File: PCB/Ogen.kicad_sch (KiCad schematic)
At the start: 17 parts, among them J1 Input, U1 PMW3360DM-T2QU, U2 TLV70019, U3 TXS0102DCU, U4 TXS0102DCU, U5 TXS0102DCU

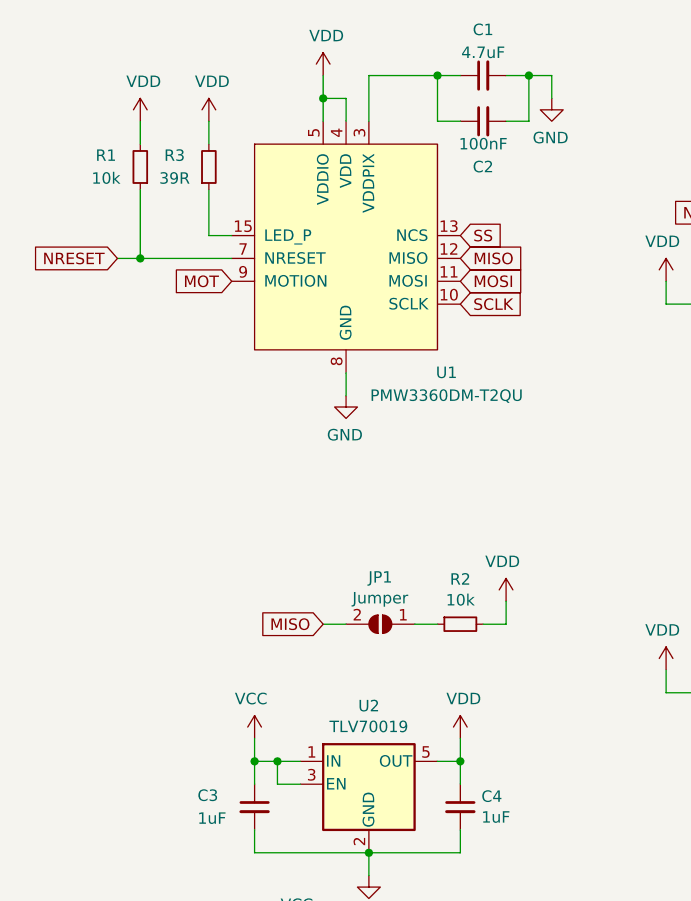
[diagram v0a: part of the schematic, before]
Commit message: ✨ ♻️ - Add metadata required to generate BOM and POS files for JLCPCB SMT assembly service (can use Fabrication Toolkit plugin to generate up to date BOM and POS). Add description to PCB and schema files. Replace TLV70019 (rupture) part by VRH1902LTX (in stock).
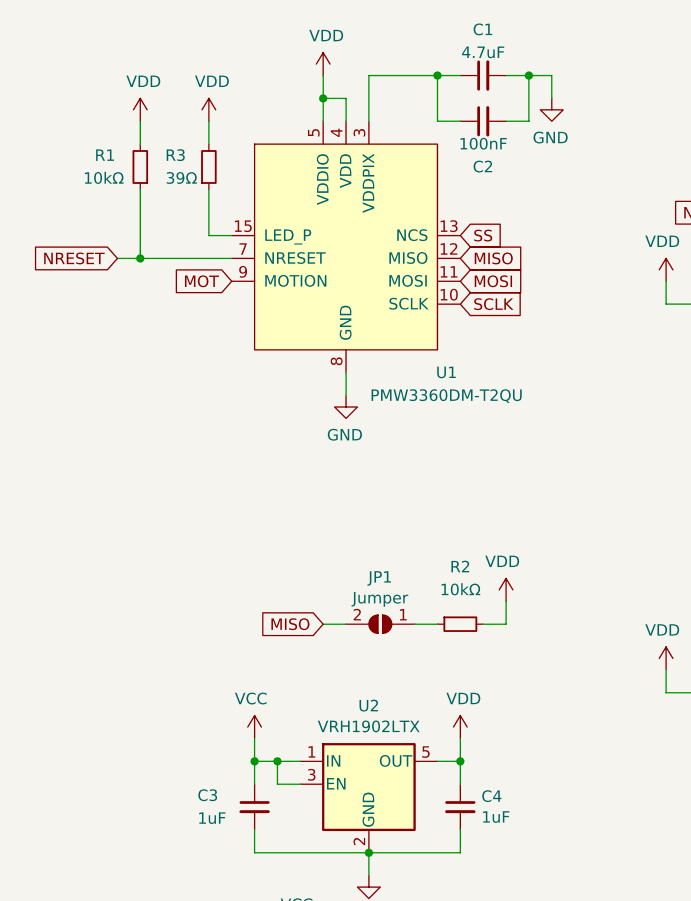
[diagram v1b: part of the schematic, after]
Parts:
- A1, H1, H2, J1, JP1: now left out of the parts list
- C1: LCSC Part # (none) -> C19666
- C2: LCSC Part # (none) -> C14663
- C3, C4: LCSC Part # (none) -> C15849
- R1, R2: value 10k -> 10kΩ; LCSC Part # (none) -> C25804
- R3: value 39R -> 39Ω; LCSC Part # (none) -> C227492
- U2: value TLV70019 -> VRH1902LTX; JLCPCB Rotation Offset (none) -> -90; LCSC Part # (none) -> C697975
- U3, U5: JLCPCB Rotation Offset (none) -> 180; LCSC Part # (none) -> C53434
- U4: JLCPCB Rotation Offset (none) -> 180; LCSC Part # (none) -> C9382C53434
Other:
- company: (none) -> Ariamelon
- title: (none) -> Ogen
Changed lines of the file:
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@@
 (kicad_sch (version 20211123) (generator eeschema)
   (paper "A4")
+  (title_block
+    (title "Ogen")
+    (date "2022-11-11")
+    (rev "V1.2")
+    (company "Ariamelon")
+  )
   (junction (at 50.8 106.68) (diameter 0) (color 0 0 0 0)
   )
@@
     (in_bom yes) (on_board yes) (fields_autoplaced)
     (property "Reference" "U2" (id 0) (at 50.8 90.3732 0))
-    (property "Value" "TLV70019" (id 1) (at 50.8 92.6846 0))
+    (property "Value" "VRH1902LTX" (id 1) (at 50.8 92.6846 0))
     (property "Footprint" "Package_TO_SOT_SMD:SOT-23-5" (id 2) (at 50.8 90.805 0)
       (effects (font (size 1.27 1.27) italic) hide)
     )
     (property "Datasheet" "http://www.ti.com/lit/ds/symlink/tlv700.pdf" (id 3) (at 50.8 97.79 0)
+      (effects (font (size 1.27 1.27)) hide)
+    )
+    (property "LCSC Part #" "C697975" (id 4) (at 50.8 99.06 0)
+      (effects (font (size 1.27 1.27)) hide)
+    )
+    (property "JLCPCB Rotation Offset" "-90" (id 5) (at 50.8 99.06 0)
       (effects (font (size 1.27 1.27)) hide)
     )
@@
   )
   (symbol (lib_id "Device:R_Small") (at 25.4 30.48 180) (unit 1)
-    (in_bom yes) (on_board yes) (fields_autoplaced)
-    (property "Reference" "R1" (id 0) (at 21.59 29.2099 0))
-    (property "Value" "10k" (id 1) (at 21.59 31.7499 0))
+    (in_bom yes) (on_board yes)
+    (property "Reference" "R1" (id 0) (at 20.32 29.21 0)
+      (effects (font (size 1.27 1.27)) (justify right))
+    )
+    (property "Value" "10kΩ" (id 1) (at 19.05 31.75 0)
+      (effects (font (size 1.27 1.27)) (justify right))
+    )
     (property "Footprint" "Resistor_SMD:R_0603_1608Metric" (id 2) (at 25.4 30.48 0)
       (effects (font (size 1.27 1.27)) hide)
     )
     (property "Datasheet" "~" (id 3) (at 25.4 30.48 0)
+      (effects (font (size 1.27 1.27)) hide)
+    )
+    (property "LCSC Part #" "C25804" (id 4) (at 25.4 30.48 0)
       (effects (font (size 1.27 1.27)) hide)
     )
@@
       (effects (font (size 1.27 1.27)) hide)
     )
+    (property "LCSC Part #" "C15849" (id 4) (at 60.96 101.6 0)
+      (effects (font (size 1.27 1.27)) hide)
+    )
     (pin "1")
     (pin "2")
@@
     )
     (property "Datasheet" "~" (id 3) (at 38.1 101.6 0)
+      (effects (font (size 1.27 1.27)) hide)
+    )
+    (property "LCSC Part #" "C15849" (id 4) (at 38.1 101.6 0)
       (effects (font (size 1.27 1.27)) hide)
     )
@@
       (effects (font (size 1.27 1.27)) hide)
     )
+    (property "LCSC Part #" "C19666" (id 4) (at 63.5 20.32 90)
+      (effects (font (size 1.27 1.27)) hide)
+    )
     (pin "1")
     (pin "2")
@@
       (effects (font (size 1.27 1.27)) hide)
     )
+    (property "LCSC Part #" "C14663" (id 4) (at 63.5 25.4 90)
+      (effects (font (size 1.27 1.27)) hide)
+    )
     (pin "1")
     (pin "2")
   )
   (symbol (lib_id "Device:R_Small") (at 33.02 30.48 0) (mirror x) (unit 1)
-    (in_bom yes) (on_board yes) (fields_autoplaced)
-    (property "Reference" "R3" (id 0) (at 29.21 29.2099 0))
-    (property "Value" "39R" (id 1) (at 29.21 31.7499 0))
+    (in_bom yes) (on_board yes)
+    (property "Reference" "R3" (id 0) (at 30.48 29.21 0)
+      (effects (font (size 1.27 1.27)) (justify right))
+    )
+    (property "Value" "39Ω" (id 1) (at 31.75 31.75 0)
+      (effects (font (size 1.27 1.27)) (justify right))
+    )
     (property "Footprint" "Resistor_SMD:R_0603_1608Metric" (id 2) (at 33.02 30.48 0)
       (effects (font (size 1.27 1.27)) hide)
@@
       (effects (font (size 1.27 1.27)) hide)
     )
+    (property "LCSC Part #" "C227492" (id 4) (at 33.02 30.48 0)
+      (effects (font (size 1.27 1.27)) hide)
+    )
     (pin "1")
     (pin "2")
   )
   (symbol (lib_id "Connector_Generic:Conn_01x08") (at 35.56 127 0) (mirror y) (unit 1)
-    (in_bom yes) (on_board yes) (fields_autoplaced)
+    (in_bom no) (on_board yes) (fields_autoplaced)
     (property "Reference" "J1" (id 0) (at 33.528 127.2032 0)
       (effects (font (size 1.27 1.27)) (justify left))
@@
   )
   (symbol (lib_id "Jumper:SolderJumper_2_Open") (at 52.07 81.28 0) (mirror y) (unit 1)
-    (in_bom yes) (on_board yes)
+    (in_bom no) (on_board yes)
     (property "Reference" "JP1" (id 0) (at 52.07 76.073 0))
     (property "Value" "Jumper" (id 1) (at 52.07 78.3844 0))
@@
   (symbol (lib_id "Device:R_Small") (at 60.96 81.28 90) (mirror x) (unit 1)
     (in_bom yes) (on_board yes) (fields_autoplaced)
-    (property "Reference" "R2" (id 0) (at 60.96 76.3016 90))
-    (property "Value" "10k" (id 1) (at 60.96 78.613 90))
+    (property "Reference" "R2" (id 0) (at 60.96 74.93 90))
+    (property "Value" "10kΩ" (id 1) (at 60.96 77.47 90))
     (property "Footprint" "Resistor_SMD:R_0603_1608Metric" (id 2) (at 60.96 81.28 0)
       (effects (font (size 1.27 1.27)) hide)
     )
     (property "Datasheet" "~" (id 3) (at 60.96 81.28 0)
+      (effects (font (size 1.27 1.27)) hide)
+    )
+    (property "LCSC Part #" "C25804" (id 4) (at 60.96 81.28 90)
       (effects (font (size 1.27 1.27)) hide)
     )
@@
     )
     (property "Datasheet" "http://www.ti.com/lit/gpn/txs0102" (id 3) (at 104.14 124.968 0)
+      (effects (font (size 1.27 1.27)) hide)
+    )
+    (property "LCSC Part #" "C53434" (id 4) (at 104.14 124.46 0)
+      (effects (font (size 1.27 1.27)) hide)
+    )
+    (property "JLCPCB Rotation Offset" "180" (id 5) (at 104.14 124.46 0)
       (effects (font (size 1.27 1.27)) hide)
     )
@@
       (effects (font (size 1.27 1.27)) hide)
     )
+    (property "LCSC Part #" "C9382C53434" (id 4) (at 104.14 81.28 0)
+      (effects (font (size 1.27 1.27)) hide)
+    )
+    (property "JLCPCB Rotation Offset" "180" (id 5) (at 104.14 81.28 0)
+      (effects (font (size 1.27 1.27)) hide)
+    )
     (pin "1")
     (pin "2")
@@
   )
   (symbol (lib_id "Mechanical:MountingHole") (at 147.32 30.48 0) (unit 1)
-    (in_bom yes) (on_board yes)
+    (in_bom no) (on_board yes)
     (property "Reference" "H1" (id 0) (at 147.32 25.4 0))
     (property "Value" "M2" (id 1) (at 147.32 27.305 0))
@@
     )
     (property "Datasheet" "" (id 3) (at 49.53 27.94 0)
+      (effects (font (size 1.27 1.27)) hide)
+    )
+    (property "LCSC Part #" "" (id 4) (at 48.26 38.1 0)
       (effects (font (size 1.27 1.27)) hide)
     )
@@
   )
   (symbol (lib_id "Mechanical:MountingHole") (at 162.56 30.48 0) (unit 1)
-    (in_bom yes) (on_board yes)
+    (in_bom no) (on_board yes)
     (property "Reference" "A1" (id 0) (at 162.56 25.4 0))
     (property "Value" "Art" (id 1) (at 162.56 27.305 0))
@@
     )
     (property "Datasheet" "http://www.ti.com/lit/gpn/txs0102" (id 3) (at 104.14 38.608 0)
+      (effects (font (size 1.27 1.27)) hide)
+    )
+    (property "LCSC Part #" "C53434" (id 4) (at 104.14 38.1 0)
+      (effects (font (size 1.27 1.27)) hide)
+    )
+    (property "JLCPCB Rotation Offset" "180" (id 5) (at 104.14 38.1 0)
       (effects (font (size 1.27 1.27)) hide)
     )
@@
   )
   (symbol (lib_id "Mechanical:MountingHole") (at 152.4 30.48 0) (unit 1)
-    (in_bom yes) (on_board yes)
+    (in_bom no) (on_board yes)
     (property "Reference" "H2" (id 0) (at 152.4 25.4 0))
     (property "Value" "M2" (id 1) (at 152.4 27.305 0))
@@
     )
     (path "/00000000-0000-0000-0000-00005f7592fd"
-      (reference "R1") (unit 1) (value "10k") (footprint "Resistor_SMD:R_0603_1608Metric")
+      (reference "R1") (unit 1) (value "10kΩ") (footprint "Resistor_SMD:R_0603_1608Metric")
     )
     (path "/00000000-0000-0000-0000-00005f802d7d"
-      (reference "R2") (unit 1) (value "10k") (footprint "Resistor_SMD:R_0603_1608Metric")
+      (reference "R2") (unit 1) (value "10kΩ") (footprint "Resistor_SMD:R_0603_1608Metric")
     )
     (path "/00000000-0000-0000-0000-00005f7611ea"
-      (reference "R3") (unit 1) (value "39R") (footprint "Resistor_SMD:R_0603_1608Metric")
+      (reference "R3") (unit 1) (value "39Ω") (footprint "Resistor_SMD:R_0603_1608Metric")
     )
     (path "/9f9f5d9b-06bb-42f6-b616-3ecf09dd2a02"
@@
     )
     (path "/00000000-0000-0000-0000-00005f74e9b7"
-      (reference "U2") (unit 1) (value "TLV70019") (footprint "Package_TO_SOT_SMD:SOT-23-5")
+      (reference "U2") (unit 1) (value "VRH1902LTX") (footprint "Package_TO_SOT_SMD:SOT-23-5")
     )
     (path "/bc64ccd8-78d4-4916-8b9a-4c0e570c7882"
